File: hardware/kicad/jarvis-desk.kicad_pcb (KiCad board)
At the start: 2 copper layers, 35 x 25 mm, 6 parts, among them J1 RJ12_6P6C, U1 Beetle_ESP32-C6

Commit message: Fix PCB layout: move Beetle header within board bounds
U1 (2x7 header) was at Y=12.5, causing pins 11-14 to extend past
the 25mm board edge. Moved to Y=4.88 (vertically centered).
Updated all trace routing to match new pin positions.

Verified: all components and traces within 35x25mm board outline.

Co-authored-by: Copilot <223556219+Copilot@users.noreply.github.com>
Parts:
- moved U1 7.69 mm to (24.0, 4.88)
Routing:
- net RX_DIV: track 34.1 -> 21.5 mm
- net HTX: track 29.3 -> 35.6 mm
- net VCC_5V: track 33.4 -> 30.7 mm
- net GND: track 42.1 -> 40.3 mm
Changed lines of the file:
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@@
   (footprint "Connector_PinHeader_2.54mm:PinHeader_2x07_P2.54mm_Vertical"
     (layer "F.Cu")
-    (at 25 12.5)
-    (property "Reference" "U1" (at 1.27 -10 0) (layer "F.SilkS") (effects (font (size 1 1) (thickness 0.15))))
-    (property "Value" "Beetle_ESP32-C6" (at 1.27 10 0) (layer "F.Fab") (effects (font (size 1 1) (thickness 0.15))))
+    (at 24 4.88)
+    (property "Reference" "U1" (at 1.27 -2 0) (layer "F.SilkS") (effects (font (size 1 1) (thickness 0.15))))
+    (property "Value" "Beetle_ESP32-C6" (at 1.27 17 0) (layer "F.Fab") (effects (font (size 1 1) (thickness 0.15))))
     (property "Footprint" "Connector_PinHeader_2.54mm:PinHeader_2x07_P2.54mm_Vertical" (at 0 0 0) (layer "F.Fab") (effects (font (size 1.27 1.27)) hide))
     (pad "1" thru_hole rect (at 0 0) (size 1.7 1.7) (drill 1.0) (layers "*.Cu" "*.Mask") (net 2 "VCC_5V"))
@@
     (pad "14" thru_hole oval (at 2.54 15.24) (size 1.7 1.7) (drill 1.0) (layers "*.Cu" "*.Mask") (net 0 ""))
   )
-  (segment (start 4.635 12.5) (end 4.635 6) (width 0.5) (layer "F.Cu") (net 2))
-  (segment (start 4.635 6) (end 25 6) (width 0.5) (layer "F.Cu") (net 2))
-  (segment (start 25 6) (end 25 12.5) (width 0.5) (layer "F.Cu") (net 2))
-  (segment (start 2.095 12.5) (end 2.095 19) (width 0.5) (layer "F.Cu") (net 1))
-  (segment (start 2.095 19) (end 14 19) (width 0.5) (layer "F.Cu") (net 1))
-  (segment (start 14 19) (end 14 15) (width 0.5) (layer "F.Cu") (net 1))
-  (segment (start 14 19) (end 25 19) (width 0.5) (layer "F.Cu") (net 1))
-  (segment (start 25 19) (end 25 27.74) (width 0.5) (layer "F.Cu") (net 1))
+  (segment (start 4.635 12.5) (end 4.635 3) (width 0.5) (layer "F.Cu") (net 2))
+  (segment (start 4.635 3) (end 24 3) (width 0.5) (layer "F.Cu") (net 2))
+  (segment (start 24 3) (end 24 4.88) (width 0.5) (layer "F.Cu") (net 2))
+  (segment (start 2.095 12.5) (end 2.095 22) (width 0.5) (layer "F.Cu") (net 1))
+  (segment (start 2.095 22) (end 14 22) (width 0.5) (layer "F.Cu") (net 1))
+  (segment (start 14 22) (end 14 15) (width 0.5) (layer "F.Cu") (net 1))
+  (segment (start 14 22) (end 24 22) (width 0.5) (layer "F.Cu") (net 1))
+  (segment (start 24 22) (end 24 20.12) (width 0.5) (layer "F.Cu") (net 1))
   (segment (start 3.365 12.5) (end 3.365 10) (width 0.25) (layer "F.Cu") (net 3))
   (segment (start 3.365 10) (end 12 10) (width 0.25) (layer "F.Cu") (net 3))
@@
   (segment (start 16 10) (end 16 15) (width 0.25) (layer "F.Cu") (net 5))
   (segment (start 16 15) (end 12 15) (width 0.25) (layer "F.Cu") (net 5))
-  (segment (start 16 10) (end 16 8) (width 0.25) (layer "F.Cu") (net 5))
-  (segment (start 16 8) (end 25 8) (width 0.25) (layer "F.Cu") (net 5))
-  (segment (start 25 8) (end 25 20.12) (width 0.25) (layer "F.Cu") (net 5))
-  (segment (start 5.905 12.5) (end 5.905 22) (width 0.25) (layer "F.Cu") (net 4))
-  (segment (start 5.905 22) (end 20 22) (width 0.25) (layer "F.Cu") (net 4))
-  (segment (start 20 22) (end 20 22.66) (width 0.25) (layer "F.Cu") (net 4))
-  (segment (start 20 22.66) (end 25 22.66) (width 0.25) (layer "F.Cu") (net 4))
+  (segment (start 16 10) (end 20 10) (width 0.25) (layer "F.Cu") (net 5))
+  (segment (start 20 10) (end 20 12.5) (width 0.25) (layer "F.Cu") (net 5))
+  (segment (start 20 12.5) (end 24 12.5) (width 0.25) (layer "F.Cu") (net 5))
+  (segment (start 5.905 12.5) (end 5.905 22.5) (width 0.25) (layer "F.Cu") (net 4))
+  (segment (start 5.905 22.5) (end 21 22.5) (width 0.25) (layer "F.Cu") (net 4))
+  (segment (start 21 22.5) (end 21 15.04) (width 0.25) (layer "F.Cu") (net 4))
+  (segment (start 21 15.04) (end 24 15.04) (width 0.25) (layer "F.Cu") (net 4))
   (zone
     (net 1)

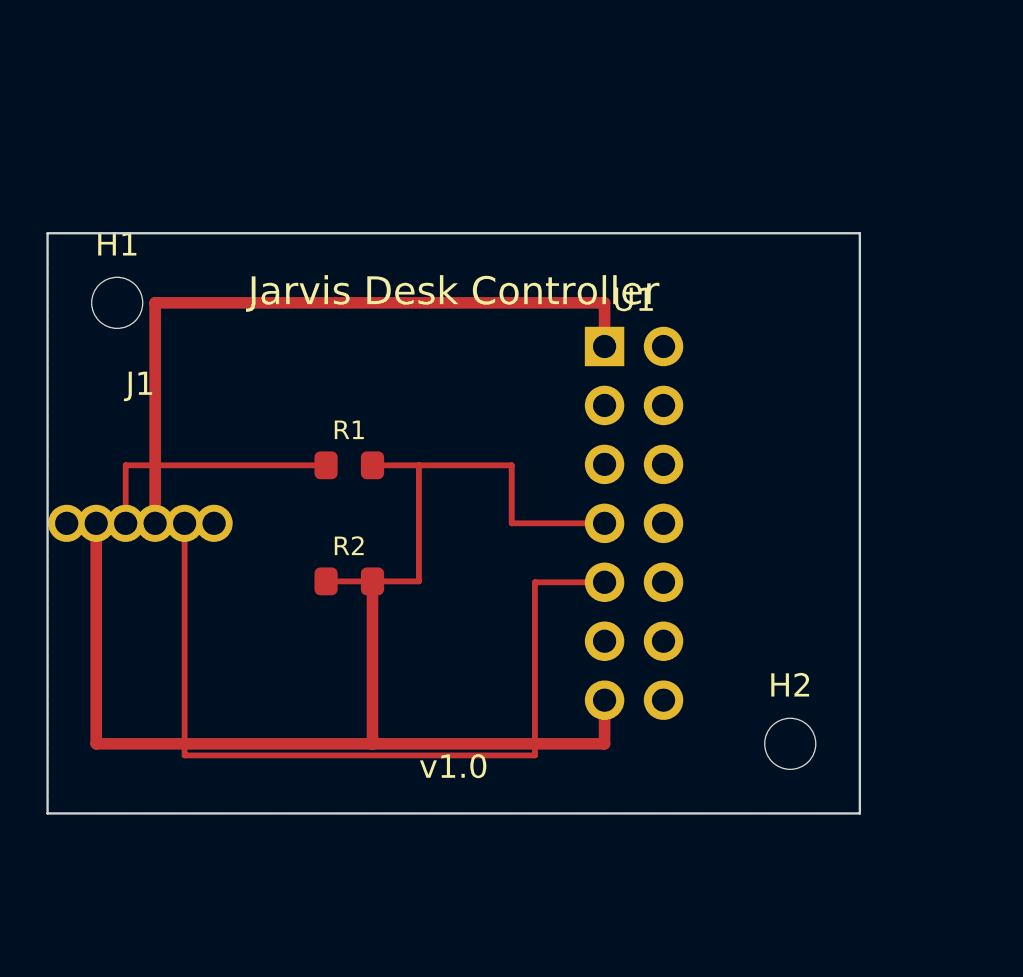
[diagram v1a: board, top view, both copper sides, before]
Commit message: Rebuild PCB with official DFRobot Beetle ESP32-C6 footprint
- Copy official kicad_mod and kicad_sym from DFRobot to hardware/kicad/libs/
- Rewrite PCB (38x30mm board) using official 16-pin Beetle footprint
  with correct pad positions (2x8, 2.54mm pitch, 17.78mm row spacing)
- Update schematic to use official Beetle_ESP32-C6 symbol
- Route all nets: GND, VCC_5V, DTX→R1→R2 voltage divider→GPIO17,
  HTX→GPIO16, with back copper GND pour
- Change DESK_TX_PIN from 18 to 16 in config.h and config.example.h
  (GPIO18 not on Beetle headers; GPIO16 is pin 12, adjacent to GPIO17)
- Pin assignments: GPIO17 (pin 13) = RX, GPIO16 (pin 12) = TX

Co-authored-by: Copilot <223556219+Copilot@users.noreply.github.com>
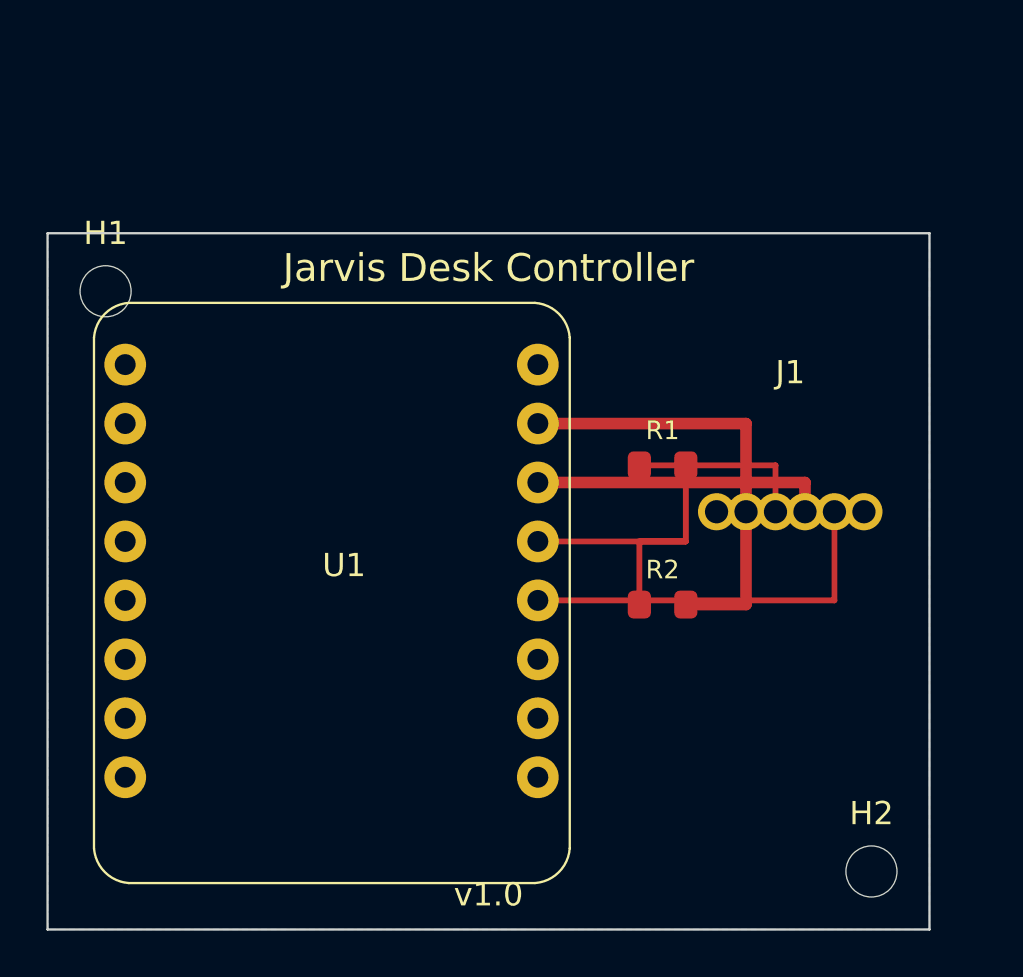
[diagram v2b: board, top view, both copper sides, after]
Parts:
- U1: footprint Connector_PinHeader_2.54mm:PinHeader_2x07_P2.54mm_Vertical -> libs:Beetle_ESP32-C6
- moved U1 31.9 mm to (2.00, 28.0)
- moved J1 28.0 mm to (32.0, 12.0)
- moved R2 13.5 mm to (26.5, 16.0)
- moved R1 13.5 mm to (26.5, 10.0)
- moved H2 6.52 mm to (35.5, 27.5)
- moved H1 0.71 mm to (2.50, 2.50)
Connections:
- U1 pad 1: VCC_5V -> GND
- U1 pad 12: (no net) -> HTX
- U1 pad 13: GND -> RX_DIV
- U1 pad 14: (no net) -> VCC_5V
- U1 pad 7: RX_DIV -> (no net)
- U1 pad 9: HTX -> (no net)
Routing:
- net GND: track 40.3 -> 19.4 mm
- net HTX: track 35.6 -> 16.6 mm
- net VCC_5V: track 30.7 -> 12.8 mm
- net RX_DIV: track 21.5 -> 14.4 mm
- net DTX: track 11.1 -> 7.86 mm
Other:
- board size 35 x 25 mm -> 38 x 30 mm

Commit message: Fix PCB layout orientation and update case to match
- Board: 40mm × 25mm landscape (was 38×30)
- Beetle ESP32-C6 at (28, 12.5) with 90° CW rotation, USB-C facing right edge
- RJ-12 connector at (5, 12.5) on left edge
- R1 at (16, 10), R2 at (16, 14) between connectors
- Mounting holes at (3, 3) and (37, 22)
- Removed manual trace routing (route in KiCad after verifying pad positions)
- Updated case.scad: RJ-12 cutout on -X (left), USB-C cutout on +X (right)
- Removed KiCad backup zip from repo

Co-authored-by: Copilot <223556219+Copilot@users.noreply.github.com>
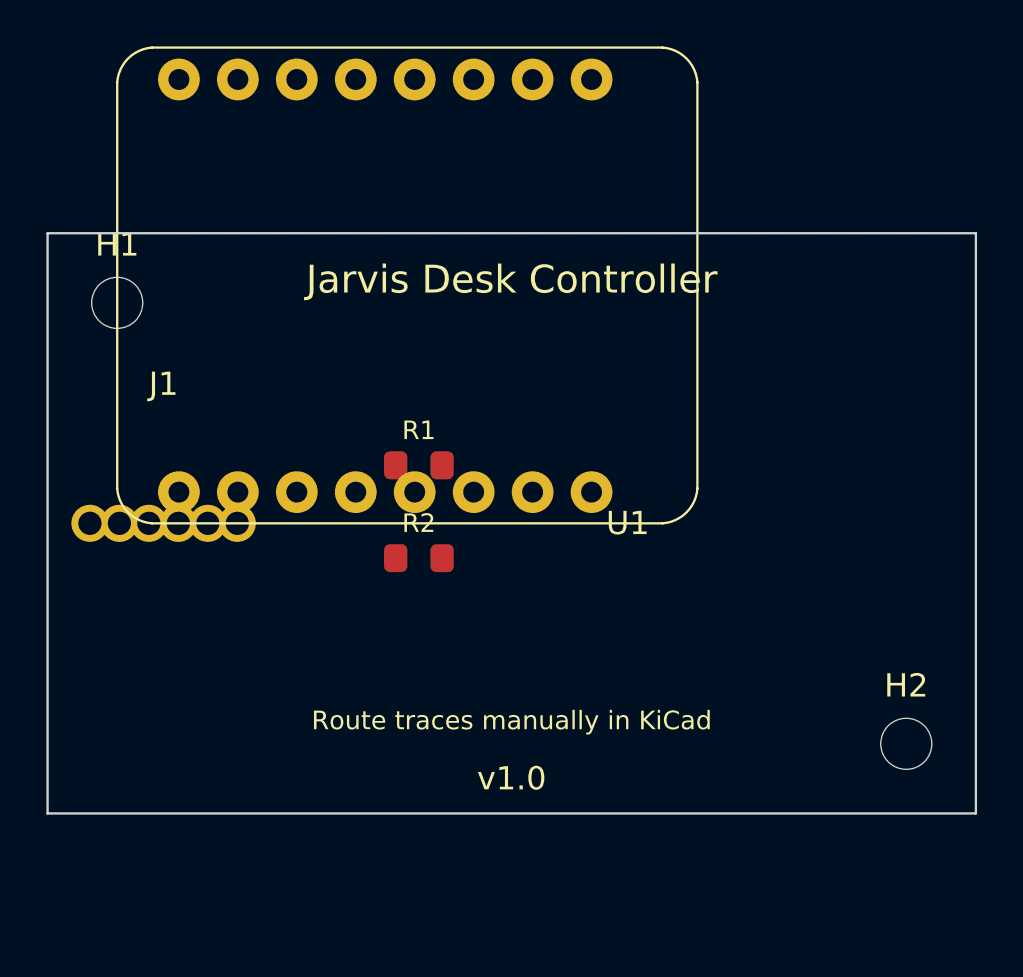
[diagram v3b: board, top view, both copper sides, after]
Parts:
- moved U1 30.3 mm to (28.0, 12.5), turned to 90 degrees
- moved J1 27.0 mm to (5.00, 12.5)
- moved R2 10.7 mm to (16.0, 14.0)
- moved R1 10.5 mm to (16.0, 10.0)
- moved H2 5.70 mm to (37.0, 22.0)
- moved H1 0.71 mm to (3.00, 3.00)
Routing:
- net GND: track 19.4 -> 0.00 mm
- net HTX: track 16.6 -> 0.00 mm
- net RX_DIV: track 14.4 -> 0.00 mm
- net VCC_5V: track 12.8 -> 0.00 mm
- net DTX: track 7.86 -> 0.00 mm
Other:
- board size 38 x 30 mm -> 40 x 25 mm
- board text added: "Route traces manually in KiCad"
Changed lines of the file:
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@@
   (net 4 "HTX")
   (net 5 "RX_DIV")
-  (gr_line (start 0 0) (end 38 0) (stroke (width 0.1) (type solid)) (layer "Edge.Cuts"))
-  (gr_line (start 38 0) (end 38 30) (stroke (width 0.1) (type solid)) (layer "Edge.Cuts"))
-  (gr_line (start 38 30) (end 0 30) (stroke (width 0.1) (type solid)) (layer "Edge.Cuts"))
-  (gr_line (start 0 30) (end 0 0) (stroke (width 0.1) (type solid)) (layer "Edge.Cuts"))
-  (gr_text "Jarvis Desk Controller" (at 19 1.5) (layer "F.SilkS")
+  (gr_line (start 0 0) (end 40 0) (stroke (width 0.1) (type solid)) (layer "Edge.Cuts"))
+  (gr_line (start 40 0) (end 40 25) (stroke (width 0.1) (type solid)) (layer "Edge.Cuts"))
+  (gr_line (start 40 25) (end 0 25) (stroke (width 0.1) (type solid)) (layer "Edge.Cuts"))
+  (gr_line (start 0 25) (end 0 0) (stroke (width 0.1) (type solid)) (layer "Edge.Cuts"))
+  (gr_text "Jarvis Desk Controller" (at 20 2) (layer "F.SilkS")
     (effects (font (size 1.2 1.2) (thickness 0.15)))
   )
-  (gr_text "v1.0" (at 19 28.5) (layer "F.SilkS")
+  (gr_text "v1.0" (at 20 23.5) (layer "F.SilkS")
     (effects (font (size 1 1) (thickness 0.12)))
+  )
+  (gr_text "Route traces manually in KiCad" (at 20 21) (layer "F.SilkS")
+    (effects (font (size 0.8 0.8) (thickness 0.1)))
   )
   (footprint "MountingHole:MountingHole_2.2mm_M2"
     (layer "F.Cu")
-    (at 2.5 2.5)
+    (at 3 3)
     (property "Reference" "H1" (at 0 -2.5 0) (layer "F.SilkS") (effects (font (size 1 1) (thickness 0.15))))
     (property "Value" "MountingHole_M2" (at 0 2.5 0) (layer "F.Fab") (effects (font (size 1 1) (thickness 0.15))))
@@
   (footprint "MountingHole:MountingHole_2.2mm_M2"
     (layer "F.Cu")
-    (at 35.5 27.5)
+    (at 37 22)
     (property "Reference" "H2" (at 0 -2.5 0) (layer "F.SilkS") (effects (font (size 1 1) (thickness 0.15))))
     (property "Value" "MountingHole_M2" (at 0 2.5 0) (layer "F.Fab") (effects (font (size 1 1) (thickness 0.15))))
@@
   (footprint "Connector_RJ:RJ12_Amphenol_54601"
     (layer "F.Cu")
-    (at 32 12)
+    (at 5 12.5)
     (property "Reference" "J1" (at 0 -6 0) (layer "F.SilkS") (effects (font (size 1 1) (thickness 0.15))))
     (property "Value" "RJ12_6P6C" (at 0 6 0) (layer "F.Fab") (effects (font (size 1 1) (thickness 0.15))))
@@
   (footprint "Resistor_SMD:R_0805_2012Metric"
     (layer "F.Cu")
-    (at 26.5 10)
+    (at 16 10)
     (property "Reference" "R1" (at 0 -1.5 0) (layer "F.SilkS") (effects (font (size 0.8 0.8) (thickness 0.12))))
     (property "Value" "1k" (at 0 1.5 0) (layer "F.Fab") (effects (font (size 0.8 0.8) (thickness 0.12))))
@@
   (footprint "Resistor_SMD:R_0805_2012Metric"
     (layer "F.Cu")
-    (at 26.5 16)
+    (at 16 14)
     (property "Reference" "R2" (at 0 -1.5 0) (layer "F.SilkS") (effects (font (size 0.8 0.8) (thickness 0.12))))
     (property "Value" "2k" (at 0 1.5 0) (layer "F.Fab") (effects (font (size 0.8 0.8) (thickness 0.12))))
@@
   (footprint "libs:Beetle_ESP32-C6"
     (layer "F.Cu")
-    (at 2 28)
-    (property "Reference" "U1" (at 10.775 -13.69 0) (layer "F.SilkS") (effects (font (size 1 1) (thickness 0.15))))
-    (property "Value" "Beetle_ESP32-C6" (at 10.775 -12.19 0) (layer "F.Fab") (effects (font (size 1 1) (thickness 0.15))))
+    (at 28 12.5 90)
+    (property "Reference" "U1" (at 0 -3 0) (layer "F.SilkS") (effects (font (size 1 1) (thickness 0.15))))
+    (property "Value" "Beetle_ESP32-C6" (at 0 3 0) (layer "F.Fab") (effects (font (size 1 1) (thickness 0.15))))
     (property "Footprint" "libs:Beetle_ESP32-C6" (at 0 0 0) (layer "F.Fab") (effects (font (size 1.27 1.27)) hide))
     (attr smd)
@@
     (pad "16" thru_hole circle (at 19.125 -22.34) (size 1.8 1.8) (drill 0.9) (layers "*.Cu" "*.Mask") (net 0 ""))
   )
-  (segment (start 30.095 12) (end 30.095 8.2) (width 0.5) (layer "F.Cu") (net 1))
-  (segment (start 30.095 8.2) (end 21.125 8.2) (width 0.5) (layer "F.Cu") (net 1))
-  (segment (start 27.5 16) (end 30.095 16) (width 0.5) (layer "F.Cu") (net 1))
-  (segment (start 30.095 16) (end 30.095 12) (width 0.5) (layer "F.Cu") (net 1))
-  (segment (start 32.635 12) (end 32.635 10.74) (width 0.5) (layer "F.Cu") (net 2))
-  (segment (start 32.635 10.74) (end 21.125 10.74) (width 0.5) (layer "F.Cu") (net 2))
-  (segment (start 31.365 12) (end 31.365 10) (width 0.25) (layer "F.Cu") (net 3))
-  (segment (start 31.365 10) (end 25.5 10) (width 0.25) (layer "F.Cu") (net 3))
-  (segment (start 33.905 12) (end 33.905 15.82) (width 0.25) (layer "F.Cu") (net 4))
-  (segment (start 33.905 15.82) (end 21.125 15.82) (width 0.25) (layer "F.Cu") (net 4))
-  (segment (start 27.5 10) (end 27.5 13.28) (width 0.25) (layer "F.Cu") (net 5))
-  (segment (start 27.5 13.28) (end 21.125 13.28) (width 0.25) (layer "F.Cu") (net 5))
-  (segment (start 27.5 13.28) (end 25.5 13.28) (width 0.25) (layer "F.Cu") (net 5))
-  (segment (start 25.5 13.28) (end 25.5 16) (width 0.25) (layer "F.Cu") (net 5))
   (zone
     (net 1)
@@
     (polygon
       (pts
-        (xy 0 0) (xy 38 0) (xy 38 30) (xy 0 30)
+        (xy 0 0) (xy 40 0) (xy 40 25) (xy 0 25)
       )
     )

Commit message: Fix Beetle placement: move left 1mm to prevent board overhang
Beetle at (27,12.5,90) — body now spans X=14.5-39.5 (within 40mm board).
Full dimensional audit passed: all components within bounds, case cutouts
aligned, mounting holes match case posts.

Co-authored-by: Copilot <223556219+Copilot@users.noreply.github.com>
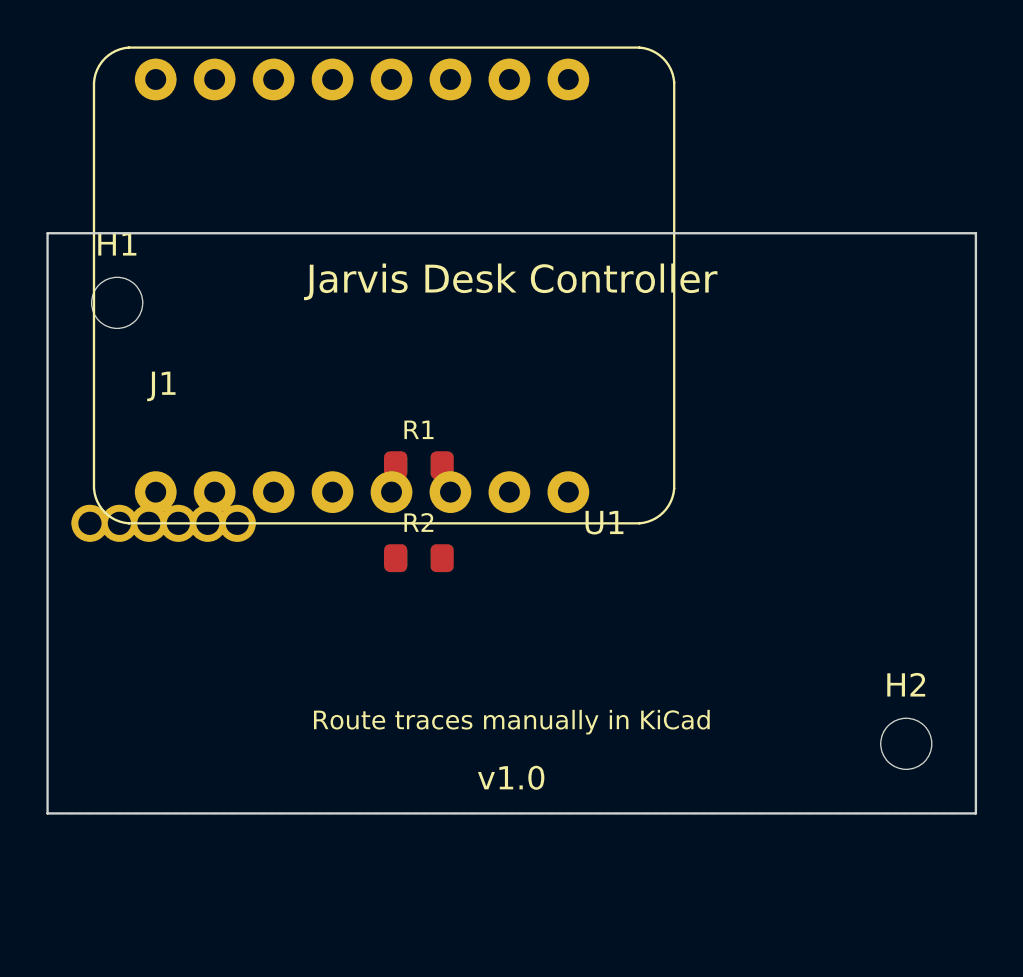
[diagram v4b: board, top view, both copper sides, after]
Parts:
- moved U1 1.00 mm to (27.0, 12.5)
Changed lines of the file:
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@@
   (footprint "libs:Beetle_ESP32-C6"
     (layer "F.Cu")
-    (at 28 12.5 90)
+    (at 27 12.5 90)
     (property "Reference" "U1" (at 0 -3 0) (layer "F.SilkS") (effects (font (size 1 1) (thickness 0.15))))
     (property "Value" "Beetle_ESP32-C6" (at 0 3 0) (layer "F.Fab") (effects (font (size 1 1) (thickness 0.15))))
